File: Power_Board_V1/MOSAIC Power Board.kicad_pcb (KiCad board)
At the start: 2 copper layers, 89.5 x 92 mm, 36 parts, among them J1 CONN E, J10 CONN 2MM JST, J11 CONN 2MM JST, J12 CONN 2MM JST, J13 CONN 2MM JST, J14 CONN 2MM JST, J15 CONN 2MM JST, J16 CONN_JST_BATT, J2 CONN_QWIIC, J3 CONN_JST_BATT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

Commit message: More fixing of libraries
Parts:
- J10, J11, J12, J13, J14, J15, J4, J5, J6, J7, J8, J9: footprint MOSAIC_Power_Board:CONN_S2B-PH-SM4-TB_JST -> power_board_footprints_V1.0:CONN_S2B-PH-SM4-TB_JST
- moved D2 77.6 mm to (192.6, 89.5)
- moved BT1 77.6 mm to (212.0, 100.5)
- moved D1 77.6 mm to (245.9, 115.9)
- moved D3 77.6 mm to (245.9, 84.5)
- moved D4 77.6 mm to (192.5, 109.0)
- moved D5 77.6 mm to (245.9, 105.0)
- moved D6 77.6 mm to (245.9, 94.5)
- moved H1 77.6 mm to (213.0, 94.0)
- moved J1 77.6 mm to (209.0, 114.2)
- moved J10 77.6 mm to (183.0, 106.5)
- moved J11 77.6 mm to (183.0, 93.0)
- moved J16 77.6 mm to (249.0, 65.5)
- moved J2 77.6 mm to (252.5, 62.0)
- moved J3 77.6 mm to (254.1, 138.0)
- moved REF** 77.6 mm to (250.8, 136.5)
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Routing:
- net /CONT_SDA: track 293.4 -> 0.00 mm, vias 12 -> 0
- net VIN: track 292.4 -> 0.00 mm, vias 11 -> 0
- net /CONT_SCL: track 284.4 -> 0.00 mm, vias 10 -> 0
- net /BATT OUT +: track 158.4 -> 0.00 mm, vias 4 -> 0
- net /SOLAR_IN: track 148.6 -> 0.00 mm, vias 5 -> 0
- net /BATT OUT -: track 144.6 -> 0.00 mm
- net GND: track 98.5 -> 0.00 mm, vias 49 -> 0
- net Net-(U3-VIN+): track 88.1 -> 0.00 mm, vias 1 -> 0
- net Net-(U4-VIN+): track 78.4 -> 0.00 mm, vias 9 -> 0
- net Net-(D3-A): track 71.9 -> 0.00 mm, vias 3 -> 0
- net Net-(U6-VIN+): track 64.6 -> 0.00 mm, vias 1 -> 0
- net Net-(U5-VIN+): track 53.5 -> 0.00 mm, vias 1 -> 0
- net Net-(D6-A): track 52.1 -> 0.00 mm, vias 3 -> 0
- net Net-(U7-VIN+): track 47.9 -> 0.00 mm
- net Net-(D5-A): track 46.7 -> 0.00 mm, vias 6 -> 0
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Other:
- board size 89.5 x 92 mm -> 89 x 89 mm

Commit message: Placement and routing work
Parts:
- removed the REF** at (249.5, 61.5)
- removed the REF** at (178.2, 142.8)
- added H10: MountingHole_Pad, power_board_footprints_V1.0:MountingHole_3.2mm_Pad_Oval, F.Cu at (116.9, 59.5)
- added H7: MountingHole_Pad, MountingHole:MountingHole_3.2mm_M3_Pad, F.Cu at (116.9, 134.5)
- added H8: MountingHole_Pad, MountingHole:MountingHole_3.2mm_M3_Pad, F.Cu at (41.9, 134.5)
- added H9: MountingHole_Pad, power_board_footprints_V1.0:MountingHole_3.2mm_Pad_Oval, F.Cu at (41.9, 59.5)
- BT1: footprint MOSAIC_Power_Board:SparkFun Lithium Ion Battery - 6Ah -> power_board_footprints_V1.0:SparkFun Lithium Ion Battery - 2Ah
- D1, D2, D3, D4, D5, D6: footprint MOSAIC_Power_Board:D_SOD-323 -> Diode_SMD:D_SOD-323
- J1: footprint MOSAIC_Power_Board:M.2-CONNECTOR-E -> power_board_footprints_V1.0:M.2-CONNECTOR-E
- J15: moved to F.Cu
- J16, J3: footprint MOSAIC_Power_Board:JST-2-SMD -> power_board_footprints_V1.0:JST-2-SMD
- J2: footprint MOSAIC_Power_Board:JST04_1MM_RA -> power_board_footprints_V1.0:JST04_1MM_RA
- J5, J9: moved to B.Cu
- TP1, TP2: footprint MOSAIC_Power_Board:PAD.03X.05 -> power_board_footprints_V1.0:PAD.03X.05
- U1, U2, U3, U4, U6, U7: footprint MOSAIC_Power_Board:INA219 Breakout -> power_board_footprints_V1.0:INA219 Breakout
- U5: footprint MOSAIC_Power_Board:INA219 Breakout -> power_board_footprints_V1.0:INA219 Breakout; moved to B.Cu
- moved U1 177.3 mm to (55.1, 58.4), turned to 0 degrees
- moved U2 166.8 mm to (55.1, 78.9), turned to 0 degrees
- moved U7 150.0 mm to (83.2, 90.0), turned to 0 degrees
- moved U3 144.7 mm to (55.1, 99.4), turned to 0 degrees
- moved U5 143.7 mm to (55.1, 78.8), turned to 0 degrees
- moved U4 141.5 mm to (55.1, 119.9)
- moved U6 141.3 mm to (83.2, 69.5), turned to 0 degrees
- moved J11 139.6 mm to (45.0, 113.4)
- moved J10 138.9 mm to (45.0, 122.4)
- moved J3 137.0 mm to (132.7, 74.5)
- moved BT1 132.6 mm to (79.5, 104.4)
- moved H1 115.8 mm to (99.0, 114.0)
- moved J1 115.8 mm to (95.0, 134.2)
- moved J2 107.8 mm to (153.6, 105.0)
- moved J16 94.3 mm to (157.3, 87.4)
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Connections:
- U2 pad 1: VIN -> unconnected-(U2-VIN-Pad1)
- U2 pad 5: /SOLAR_IN -> unconnected-(U2-VIN--Pad5)
- U2 pad 6: /BATT OUT + -> unconnected-(U2-VIN+-Pad6)

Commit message: Placement and routing work
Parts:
- D4: moved to B.Cu
- J3, TP1, TP2: moved to F.Cu
- moved D1 173.5 mm to (79.0, 68.5), turned to -90 degrees
- moved D3 173.1 mm to (79.0, 130.4)
- moved D5 143.7 mm to (104.5, 79.5), turned to -90 degrees
- moved D6 141.5 mm to (104.5, 100.0)
- moved D4 131.1 mm to (72.4, 56.4)
- moved D2 115.4 mm to (79.0, 109.9), turned to -90 degrees
- moved J16 110.1 mm to (47.3, 82.3)
- moved TP1 104.2 mm to (116.4, 73.4), turned to 180 degrees
- moved TP2 99.1 mm to (116.4, 79.4), turned to 180 degrees
- moved J2 43.0 mm to (113.8, 88.8)
- moved J3 32.2 mm to (115.4, 101.7), turned to -90 degrees
- moved BT1 0.71 mm to (78.8, 104.4)

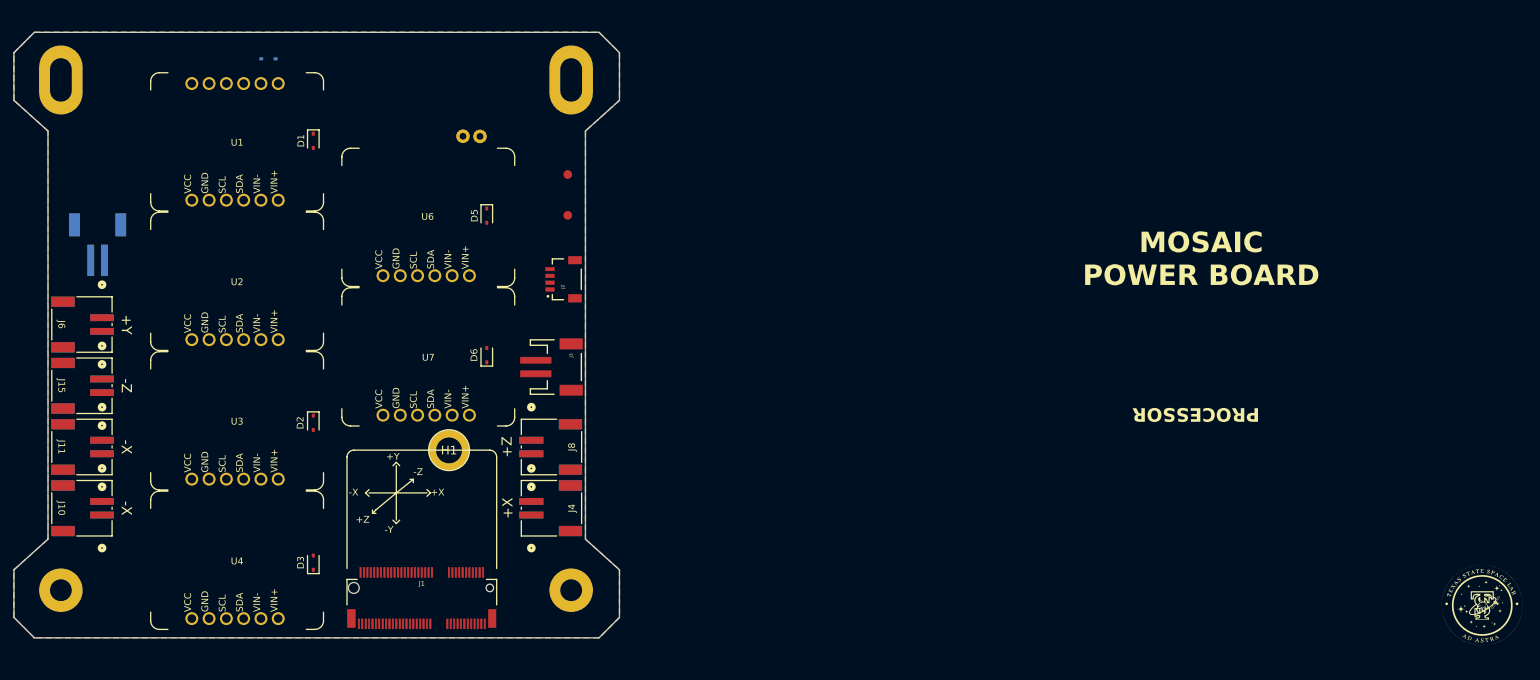
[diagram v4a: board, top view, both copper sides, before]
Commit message: Finished placement and tracing
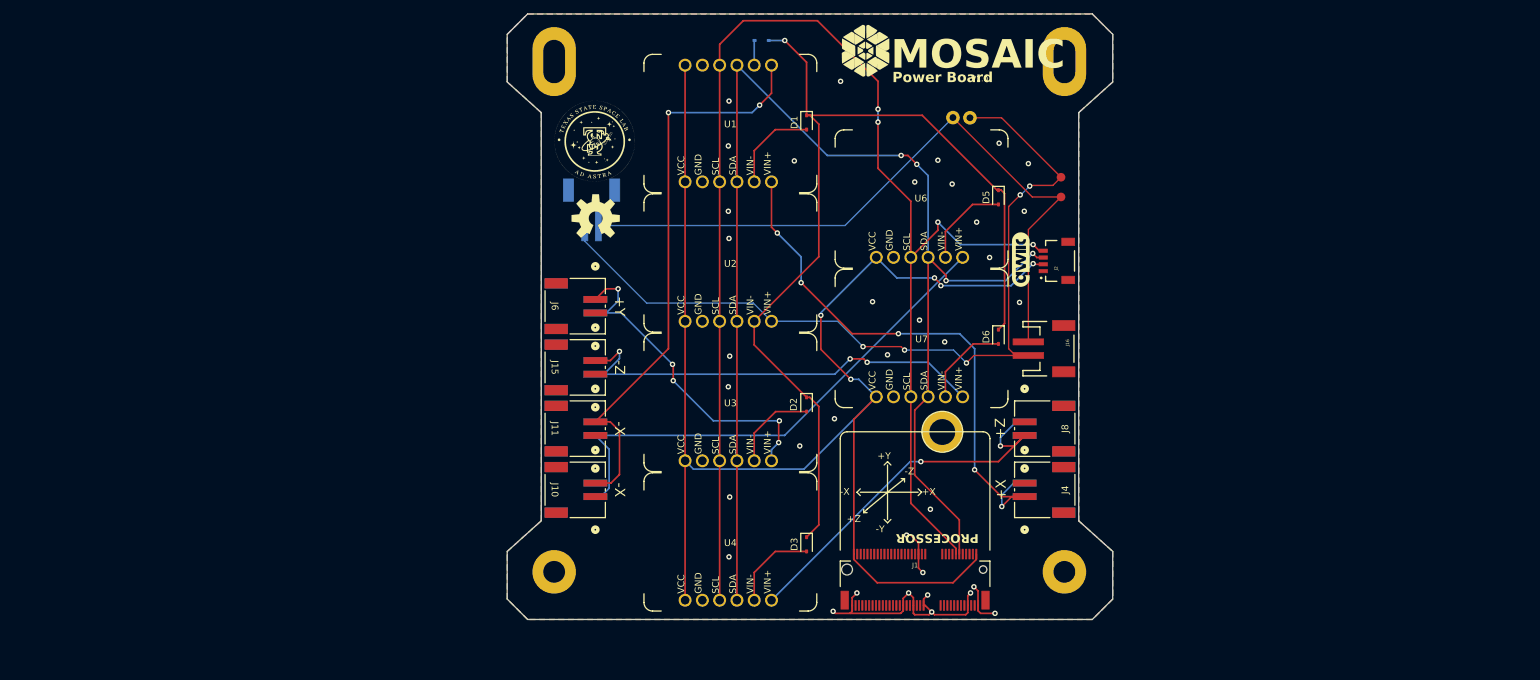
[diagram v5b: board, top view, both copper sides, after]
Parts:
- added G***: LOGO, LOGO, F.Cu at (160.1, 55.2)
- added LOGO1: QWIIC_LOGO_8MM, power_board_footprints_V1.0:QWIIC_8MM, F.Cu at (183.0, 85.9)
- added LOGO2: OSHW-LOGOL, power_board_footprints_V1.0:OSHW-LOGO-L, F.Cu at (120.5, 79.8)
- H1: footprint MOSAIC_Power_Board:STAND-OFF-REFLOW-M2.5 -> power_board_footprints_V1.0:STAND-OFF-REFLOW-M2.5
- J16: moved to F.Cu
- J3: moved to B.Cu
- REF**: footprint MOSAIC_Power_Board:SL_Logo -> power_board_footprints_V1.0:SL_Logo
- moved REF** 147.2 mm to (120.3, 68.3)
- moved J16 141.5 mm to (187.8, 99.0), turned to -90 degrees
- moved D5 75.2 mm to (179.7, 76.8)
- moved D6 75.2 mm to (179.7, 97.2), turned to -90 degrees
- moved J4 72.6 mm to (186.5, 119.7)
- moved J5 72.6 mm to (186.5, 119.7)
- moved J8 72.6 mm to (186.5, 110.7)
- moved J9 72.6 mm to (186.5, 110.7)
- moved D1 72.6 mm to (151.5, 65.8)
- moved D2 72.6 mm to (151.5, 107.2)
- moved D3 72.6 mm to (151.5, 127.8), turned to -90 degrees
- moved D4 72.6 mm to (144.9, 53.7)
- moved H10 72.6 mm to (189.4, 56.8)
- moved H7 72.6 mm to (189.4, 131.8)
- moved H8 72.6 mm to (114.4, 131.8)
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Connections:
- J16 pad NC1: unconnected-(J16-PAD1-PadNC1) -> GND
- J16 pad NC2: unconnected-(J16-PAD2-PadNC2) -> GND
- J3 pad NC1: unconnected-(J3-PAD1-PadNC1) -> GND
- J3 pad NC2: unconnected-(J3-PAD2-PadNC2) -> GND
- U2 pad 1: unconnected-(U2-VIN-Pad1) -> VIN
- U2 pad 5: unconnected-(U2-VIN--Pad5) -> /SOLAR_IN
- U2 pad 6: unconnected-(U2-VIN+-Pad6) -> /BATT OUT +
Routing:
- net VIN: track 0.00 -> 214.2 mm, vias 0 -> 5
- net /CONT_SCL: track 0.00 -> 208.4 mm, vias 0 -> 4
- net /CONT_SDA: track 0.00 -> 193.3 mm, vias 0 -> 4
- net /SOLAR_IN: track 0.00 -> 140.8 mm, vias 0 -> 1
- net /BATT OUT +: track 0.00 -> 126.1 mm, vias 0 -> 5
- net /BATT OUT -: track 0.00 -> 102.7 mm
- net Net-(U5-VIN+): track 0.00 -> 84.9 mm, vias 0 -> 2
- net Net-(U1-VIN+): track 0.00 -> 82.7 mm, vias 0 -> 5
- net Net-(U6-VIN+): track 0.00 -> 76.0 mm
- net Net-(U7-VIN+): track 0.00 -> 66.9 mm, vias 0 -> 3
- net Net-(U4-VIN+): track 0.00 -> 57.2 mm, vias 0 -> 2
- net Net-(U3-VIN+): track 0.00 -> 51.2 mm, vias 0 -> 5
- net GND: track 0.00 -> 48.5 mm, vias 0 -> 36
- net Net-(D1-A): track 0.00 -> 13.6 mm
- net Net-(D5-A): track 0.00 -> 13.2 mm
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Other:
- board text added: "MOSAIC"
- board text added: "Power Board"
- board text added: "V1.0"
- board text removed: "MOSAIC POWER BOARD"

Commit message: Made JLCPCB production files
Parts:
- LOGO1: value QWIIC_LOGO_8MM -> ~
- LOGO2: value OSHW-LOGOL -> ~
- moved D3 16.3 mm to (136.7, 134.6)
- moved BT1 16.3 mm to (136.0, 108.5)
- moved D1 16.3 mm to (136.7, 72.5)
- moved D2 16.3 mm to (136.7, 114.0)
- moved D4 16.3 mm to (130.1, 60.5)
- moved H10 16.3 mm to (174.6, 63.6)
- moved H9 16.3 mm to (99.6, 63.6)
- moved J10 16.3 mm to (102.7, 126.5)
- moved J11 16.3 mm to (102.7, 117.5)
- moved J12 16.3 mm to (102.7, 126.5)
- moved J13 16.3 mm to (102.7, 117.5)
- moved J14 16.3 mm to (102.7, 108.5)
- moved J15 16.3 mm to (102.7, 108.5)
- moved J16 16.3 mm to (173.0, 105.8)
- moved J3 16.3 mm to (105.1, 84.0)
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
